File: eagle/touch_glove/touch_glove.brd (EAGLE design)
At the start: 76.2 x 50.8 mm, 187 parts, among them Q1 MCH3474 4A/30V/50mΩ, Q2 MCH3474 4A/30V/50mΩ, Q3 MCH3474 4A/30V/50mΩ, Q4 MCH3474 4A/30V/50mΩ, Q5 MCH3474 4A/30V/50mΩ, Q6 MCH3474 4A/30V/50mΩ, SW2 5A/28V, Y2 16MHz

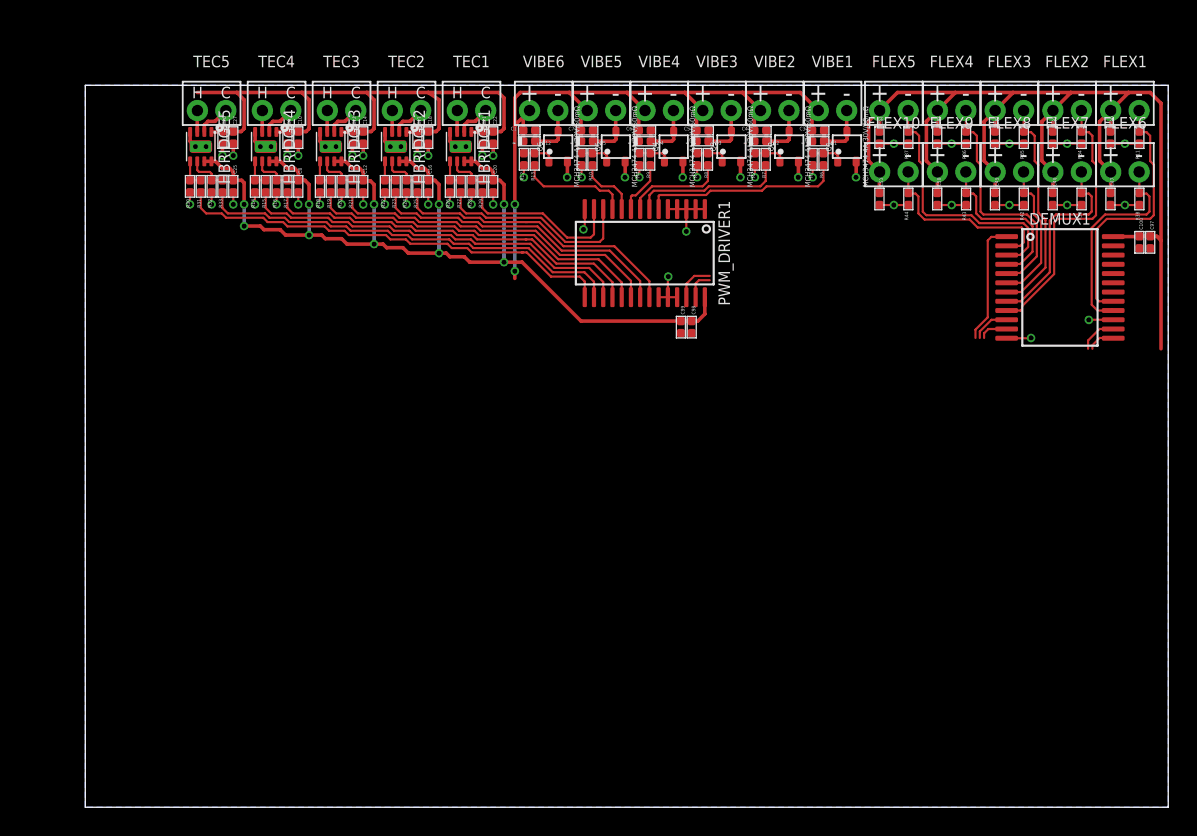
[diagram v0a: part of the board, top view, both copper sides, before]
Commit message: Touch Glove Rev 1: Resized board.  2.77in in length, under my goal of 3in
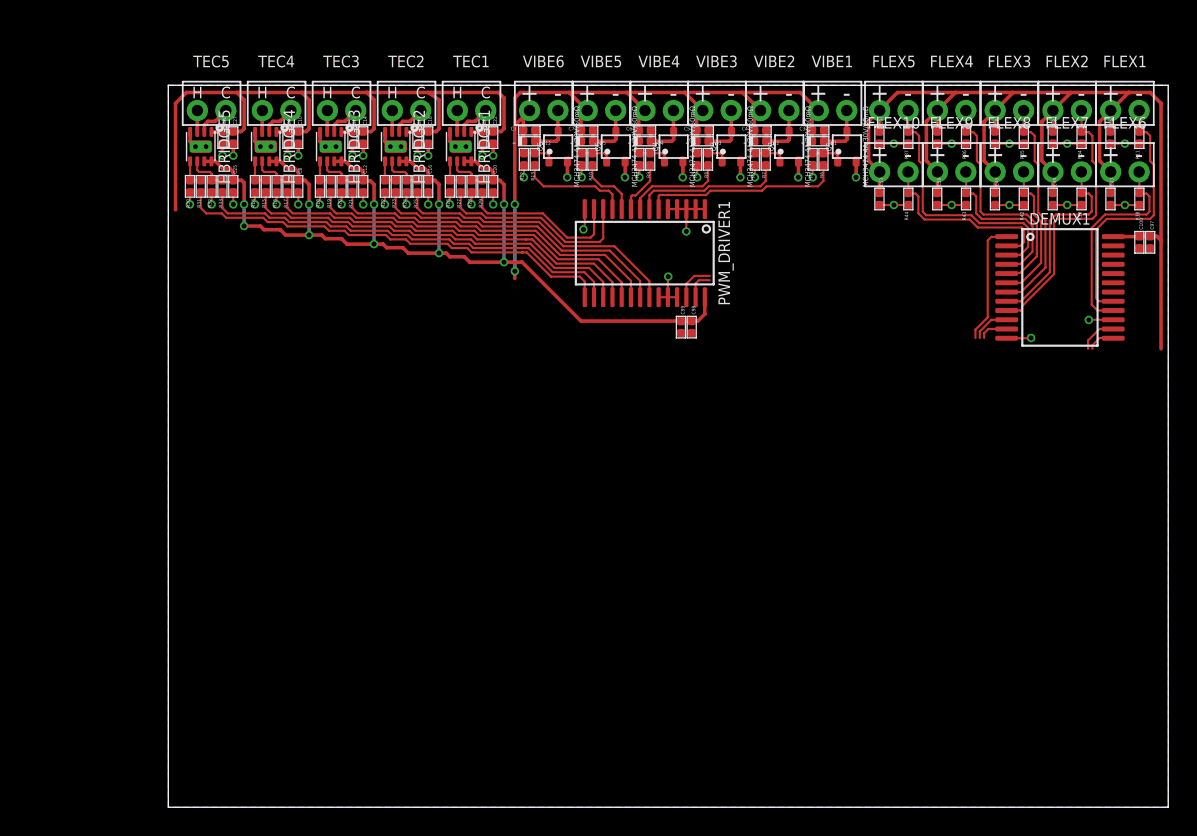
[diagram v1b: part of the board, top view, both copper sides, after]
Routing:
- net 1.8V: track 47.1 -> 56.4 mm
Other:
- board size 76.2 x 50.8 mm -> 70.4 x 50.8 mm
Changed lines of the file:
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@@
 <board>
 <plain>
-<wire x1="0" y1="0" x2="76.2" y2="0" width="0" layer="20"/>
+<wire x1="5.842" y1="0" x2="76.2" y2="0" width="0" layer="20"/>
 <wire x1="76.2" y1="0" x2="76.2" y2="50.8" width="0" layer="20"/>
-<wire x1="76.2" y1="50.8" x2="0" y2="50.8" width="0" layer="20"/>
-<wire x1="0" y1="50.8" x2="0" y2="0" width="0" layer="20"/>
+<wire x1="76.2" y1="50.8" x2="5.842" y2="50.8" width="0" layer="20"/>
+<wire x1="5.842" y1="50.8" x2="5.842" y2="0" width="0" layer="20"/>
+<dimension x1="5.842" y1="0" x2="76.2" y2="0" x3="41.021" y3="-2.794" textsize="1.778" layer="48" unit="inch"/>
 </plain>
 <attributes>
@@
 <vertex x="76.2" y="50.8"/>
 <vertex x="76.2" y="0"/>
-<vertex x="0" y="0"/>
-<vertex x="0" y="50.8"/>
+<vertex x="5.842" y="0"/>
+<vertex x="5.842" y="50.8"/>
 </polygon>
 <wire x1="51.181" y1="45.168" x2="51.181" y2="44.323" width="0.1524" layer="1"/>
@@
 <wire x1="24.13" y1="50.292" x2="29.083" y2="50.292" width="0.254" layer="1"/>
 <wire x1="15.24" y1="50.292" x2="19.812" y2="50.292" width="0.254" layer="1"/>
-<wire x1="10.668" y1="50.292" x2="15.24" y2="50.292" width="0.254" layer="1"/>
-<wire x1="10.668" y1="50.292" x2="7.874" y2="50.292" width="0.254" layer="1"/>
+<wire x1="15.24" y1="50.292" x2="10.668" y2="50.292" width="0.254" layer="1"/>
 <wire x1="29.254" y1="47.542" x2="28.702" y2="47.542" width="0.254" layer="1"/>
 <wire x1="29.254" y1="47.542" x2="29.464" y2="47.752" width="0.254" layer="1"/>
@@
 <wire x1="11.176" y1="47.752" x2="11.176" y2="49.784" width="0.254" layer="1"/>
 <wire x1="11.176" y1="49.784" x2="10.668" y2="50.292" width="0.254" layer="1"/>
-<wire x1="-33.55" y1="46.99" x2="7.874" y2="50.292" width="0" layer="19" extent="1-1"/>
+<wire x1="7.112" y1="50.292" x2="6.35" y2="49.53" width="0.254" layer="1"/>
+<wire x1="10.668" y1="50.292" x2="7.112" y2="50.292" width="0.254" layer="1"/>
+<wire x1="6.35" y1="49.53" x2="6.35" y2="42.037" width="0.254" layer="1"/>
+<wire x1="-33.55" y1="46.99" x2="6.35" y2="49.53" width="0" layer="19" extent="1-1"/>
 <wire x1="-49.955" y1="72.39" x2="-33.55" y2="46.99" width="0" layer="19" extent="1-1"/>
 <wire x1="-76.625" y1="64.77" x2="-49.955" y2="72.39" width="0" layer="19" extent="1-1"/>

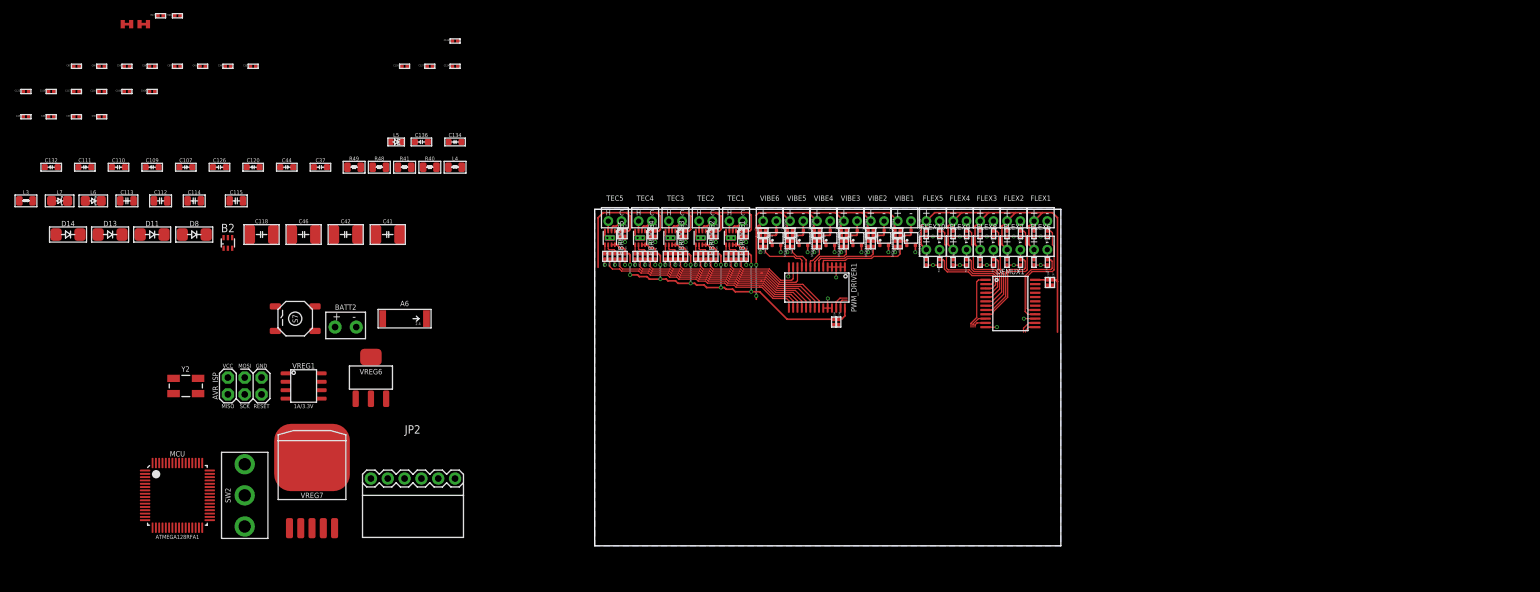
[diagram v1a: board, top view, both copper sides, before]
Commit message: Rev 1 - Touch Glove:  Completed.  Need to test several pin changes before tape out
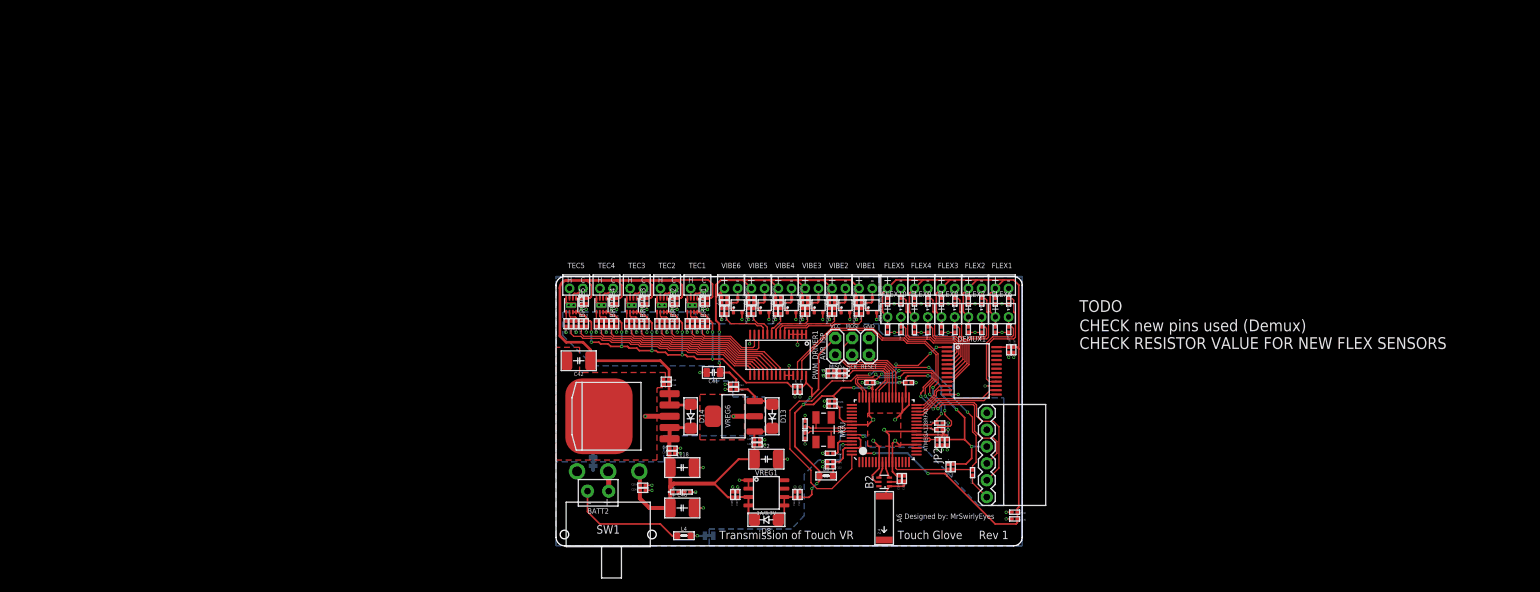
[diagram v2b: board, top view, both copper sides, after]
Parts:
- removed C35, C57, C58, C59, C60, C61: 10uF/10V, PiB_capacitors:_CER_SMD_0402
- removed L5: BLUE, PiB_leds:LED_SMD-0603_
- removed L6: GREEN, PiB_leds:LED_SMD-805_
- removed L7: RED, PiB_leds:LED_SMD-805_
- removed S7: TACTILE-SW_500mA/12V, PiB_switches:BTN_MOMENTARY_SPST-NO_SMD_12V_50MA_L5.2-W5.2
- removed SW2: 5A/28V, PiB_switches:SW_TOGGLE_SPDT_5A-28V_13L-7W
- added C2: 100uF/16V, PiB_capacitors:_CER_SMD-1210
- added LED1: GREEN, PiB_leds:LED_SMD-0402
- added LED2: RED, PiB_leds:LED_SMD-0402
- added LED3: BLUE, PiB_leds:LED_SMD-0402
- added SW1: 4A/28V, PiB_switches:SW_SLIDE_RA_SPDT_4A-28V_L12.7-W9.5
- C107, C109, C110, C111, C132, C134, C136: device PiB_capacitors:_CER_SMD-603 -> PiB_capacitors:_CER_SMD_0402
- C112, C113: value 12pF/250V -> 12pF/100V; device PiB_capacitors:_CER_SMD-805 -> PiB_capacitors:_CER_SMD_0402
- C114: value 22PF/250V -> 22pF/50V; device PiB_capacitors:_CER_SMD-805 -> PiB_capacitors:_CER_SMD_0402
- C115: value 0.75PF/100V -> 0.75pF/50V; device PiB_capacitors:_CER_SMD-805 -> PiB_capacitors:_CER_SMD_0402
- C118, C42, C46: value 100uF -> 100uF/16V
- C120, C126, C37, C44: value 10uF/16V -> 10uF/10V; device PiB_capacitors:_CER_SMD-603 -> PiB_capacitors:_CER_SMD_0402
- C41: value 100uF -> 47uF/10V; device PiB_capacitors:_CER_SMD-1210 -> PiB_capacitors:_CER_SMD-805
- D11: value 1A/50V -> 150mA/75V; device PiB_discrete_semiconductors:SOD123F -> PiB_discrete_semiconductors:SOD-923F/0402
- D13, D14: device MrSwirlyEyes:DIODE_SMD_1A-50V-SOD123F -> PiB_discrete_semiconductors:SOD123F
- L3, L4: value 10uH -> 10uH/0.38A; device PiB_inductors:_SMD-805 -> PiB_inductors:_SMD-0603
- R40, R41: value 4.7K -> 4.7KΩ; device PiB_resistors:RESISTOR_SMD-805 -> PiB_resistors:RESISTOR_SMD-0402
- R48, R49: device PiB_resistors:RESISTOR_SMD-805 -> PiB_resistors:RESISTOR_SMD-0402
- VREG7: device MrSwirlyEyes:DDPAK-5 -> PiB_ic_power:DDPAK-5
- moved C117 147.0 mm to (62.9, 11.0), turned to 90 degrees
- moved C132 140.0 mm to (57.5, 15.6), turned to 270 degrees
- moved R46 135.4 mm to (59.9, 11.9), turned to 90 degrees
- moved C122 134.0 mm to (41.4, 11.9), turned to 180 degrees
- moved C108 134.0 mm to (58.3, 15.6), turned to 270 degrees
- moved L3 127.7 mm to (40.8, 10.5)
- moved C109 127.0 mm to (59.1, 15.6), turned to 270 degrees
- moved D11 125.2 mm to (59.2, 11.9), turned to 90 degrees
- moved C116 124.0 mm to (47.4, 24.6), turned to 180 degrees
- moved C45 120.7 mm to (30.4, 16.0)
- moved C111 118.4 mm to (41.7, 21.1), turned to 180 degrees
- moved C110 115.8 mm to (41.4, 14.0), turned to 180 degrees
- moved ANALOG_BR 115.1 mm to (23.1, 1.52), flipped to the bottom, turned to 180 degrees
- moved C135 114.7 mm to (69.2, 4.06), turned to 180 degrees
- moved C114 114.4 mm to (51.8, 10.2), turned to 90 degrees
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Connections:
- removed net N$51: JP2.CTS
- net 3.3V: no longer C35.1, C57.1, C58.1, C59.1, C60.1, C61.1
- net A1: now also DEMUX1.1
- net A5: no longer DEMUX1.1
- net BATT_+: now also SW1.P; no longer SW2.2
- net GND: now also C2.2; no longer C36.2, C39.2, C40.2, C41.2, C42.2, C43.2, S7.1, VREG6.2, VREG6.TAB, VREG7.3, VREG7.TAB
- net N$53: now also LED3.K; no longer L5.2
- net N$54: now also LED1.K; no longer L6.K
- net N$55: now also LED2.K; no longer L7.K
- net NGND: now also C36.2, C39.2, C40.2, C41.2, C42.2, C43.2, VREG6.2, VREG6.TAB, VREG7.3, VREG7.TAB; no longer C35.2, C57.2, C58.2, C59.2, C60.2, C61.2
- net PB6: now also LED2.A; no longer L7.A
- net PB7: now also LED1.A; no longer L6.A
- net PD4: now also DEMUX1.13
- net PD5: now also DEMUX1.14
- net PD6: now also DEMUX1.11
- net PD7: now also DEMUX1.10
- net PE2: no longer DEMUX1.10
- net PE6: no longer DEMUX1.11
- net PE7: no longer DEMUX1.14
- net RESET: no longer S7.3
- net SSN: no longer DEMUX1.13
- net VBATT: now also C2.1, LED3.A, SW1.S1; no longer L5.1, SW2.1
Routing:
- net VCC: track 76.7 -> 180.6 mm, vias 10 -> 23
- net GND: track 21.1 -> 107.5 mm, vias 18 -> 52
- net AVCC: track 88.2 -> 146.1 mm, vias 0 -> 2
- net VBATT: track 0.00 -> 57.4 mm
- net A1: track 0.00 -> 50.7 mm, vias 0 -> 4
- net TX0: track 0.00 -> 44.0 mm, vias 0 -> 4
- net SCL: track 2.82 -> 45.0 mm, vias 0 -> 2
- net RESET: track 0.00 -> 41.1 mm, vias 0 -> 2
- net RX0: track 0.00 -> 39.9 mm, vias 0 -> 4
- net SDA: track 2.08 -> 40.8 mm, vias 0 -> 2
- net 1.8V: track 56.4 -> 85.0 mm
- net MOSI: track 0.00 -> 15.8 mm
- net NGND: track 26.1 -> 40.4 mm, vias 22 -> 27
- net PD5: track 0.00 -> 13.4 mm
- net PD4: track 0.00 -> 13.4 mm
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- added copper zone on layer 16, net AGND
- added copper zone on layer 1, net GND
- added copper zone on layer 16, net GND
- added copper zone on layer 1, net NGND
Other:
- board size 70.4 x 50.8 mm -> 70.4 x 40.6 mm
- board text added: "CHECK new pins used (Demux) CHECK RESISTOR VALUE FOR NEW FLEX SENSORS"
- board text added: "Designed by: MrSwirlyEyes"
- board text added: "TODO"
- board text added: "Touch Glove Rev 1"
- board text added: "Transmission of Touch VR"
